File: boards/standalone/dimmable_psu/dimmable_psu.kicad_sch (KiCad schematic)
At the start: 82 parts, among them J1 DIM_IN, J2 PWM_IN, J3 POWER, J4 POWER_OUT, Q1 2N7002, Q2 IRF540N, Q3 IRF540N, U1 LM324, U2 LMC7660, U3 TPS92640

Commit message: some more pcb work
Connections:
- net GND: now also U3.15 (TP)
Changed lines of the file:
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@@
+    (stroke (width 0) (type solid) (color 0 0 0 0))
+  )
+  (wire (pts (xy 278.765 113.03) (xy 278.765 114.3))
     (stroke (width 0) (type solid) (color 0 0 0 0))
   )
@@
     )
     (property "Datasheet" "" (id 3) (at 254 119.38 0)
+      (effects (font (size 1.27 1.27)) hide)
+    )
+    (pin "1")
+  )
+  (symbol (lib_id "power:GND") (at 278.765 114.3 0) (unit 1)
+    (in_bom yes) (on_board yes)
+    (property "Reference" "#PWR?" (id 0) (at 278.765 120.65 0)
+      (effects (font (size 1.27 1.27)) hide)
+    )
+    (property "Value" "GND" (id 1) (at 279.4 119.38 0)
+      (effects (font (size 1.27 1.27)) hide)
+    )
+    (property "Footprint" "" (id 2) (at 278.765 114.3 0)
+      (effects (font (size 1.27 1.27)) hide)
+    )
+    (property "Datasheet" "" (id 3) (at 278.765 114.3 0)
       (effects (font (size 1.27 1.27)) hide)
     )
@@
     (pin "8")
     (pin "9")
+  )
+  (symbol (lib_id "Regulator_SwitchedCapacitor:LMC7660") (at 222.25 247.65 0) (unit 1)
+    (in_bom yes) (on_board yes)
+    (property "Reference" "U2" (id 0) (at 222.25 232.41 0))
+    (property "Value" "LMC7660" (id 1) (at 222.25 234.95 0))
+    (property "Footprint" "Package_SO:SOIC-8_3.9x4.9mm_P1.27mm" (id 2) (at 156.21 217.17 0)
+      (effects (font (size 1.27 1.27)) hide)
+    )
+    (property "Datasheet" "http://www.ti.com/lit/ds/symlink/lmc7660.pdf" (id 3) (at 156.21 217.17 0)
+      (effects (font (size 1.27 1.27)) hide)
+    )
+    (pin "1")
+    (pin "2")
+    (pin "3")
+    (pin "4")
+    (pin "5")
+    (pin "6")
+    (pin "7")
+    (pin "8")
   )
   (symbol (lib_id "ti_reg:TPS92640") (at 278.13 100.33 0) (unit 1)
@@
     (pin "13")
     (pin "14")
-  )
-  (symbol (lib_id "Regulator_SwitchedCapacitor:LMC7660") (at 222.25 247.65 0) (unit 1)
-    (in_bom yes) (on_board yes)
-    (property "Reference" "U2" (id 0) (at 222.25 232.41 0))
-    (property "Value" "LMC7660" (id 1) (at 222.25 234.95 0))
-    (property "Footprint" "Package_SO:SOIC-8_3.9x4.9mm_P1.27mm" (id 2) (at 156.21 217.17 0)
-      (effects (font (size 1.27 1.27)) hide)
-    )
-    (property "Datasheet" "http://www.ti.com/lit/ds/symlink/lmc7660.pdf" (id 3) (at 156.21 217.17 0)
-      (effects (font (size 1.27 1.27)) hide)
-    )
-    (pin "1")
-    (pin "2")
-    (pin "3")
-    (pin "4")
-    (pin "5")
-    (pin "6")
-    (pin "7")
-    (pin "8")
+    (pin "15")
   )
   (sheet_instances
@@
       (reference "#PWR0102") (unit 1) (value "GND") (footprint "")
     )
+    (path "/b43fa32d-11e5-4e08-bf48-f76538006246"
+      (reference "#PWR?") (unit 1) (value "GND") (footprint "")
+    )
     (path "/ce8d3fd1-9e4e-41e4-802c-895ac6841362"

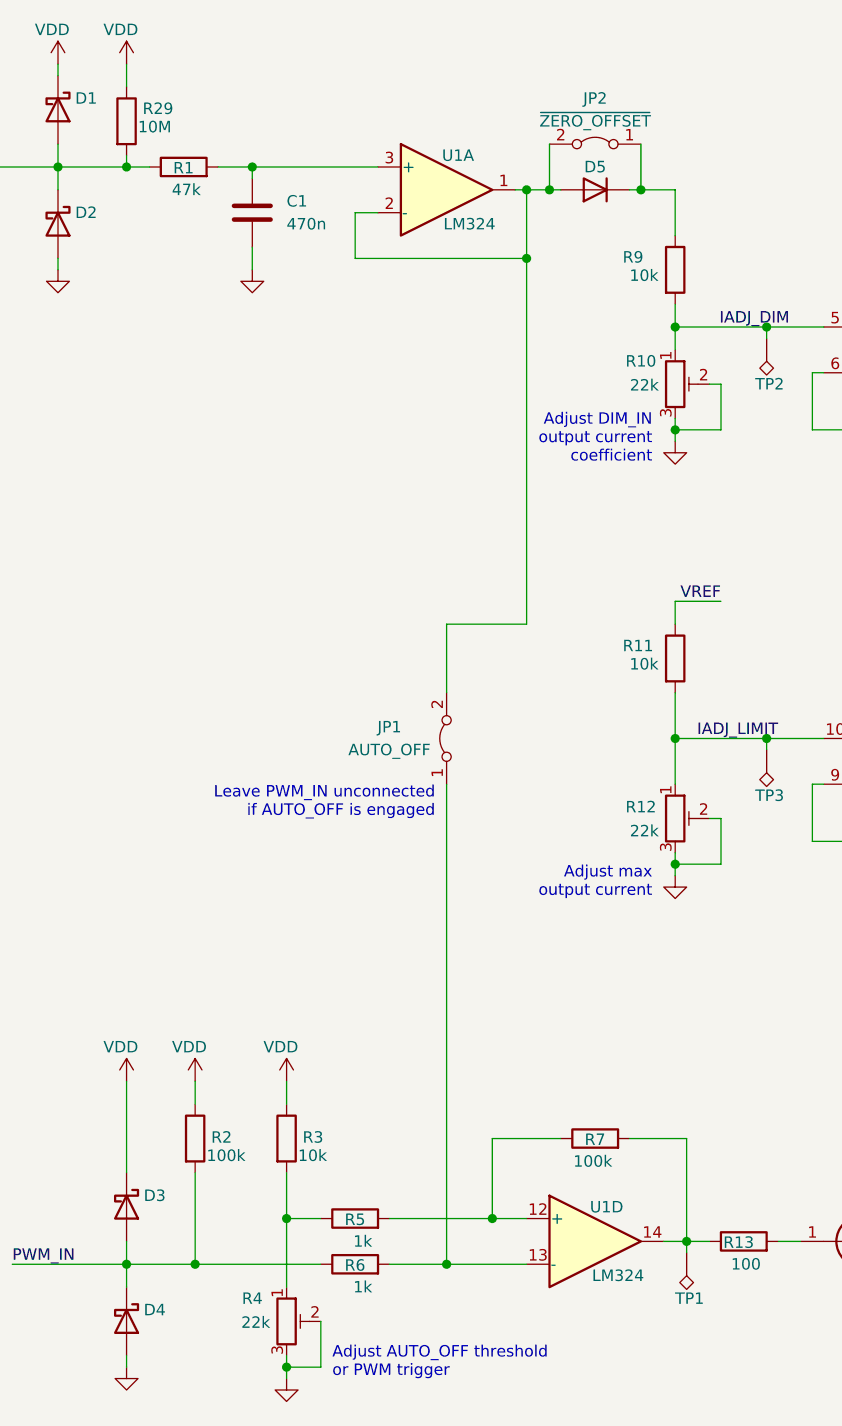
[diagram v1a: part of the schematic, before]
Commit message: use dip switches instead of jumpers
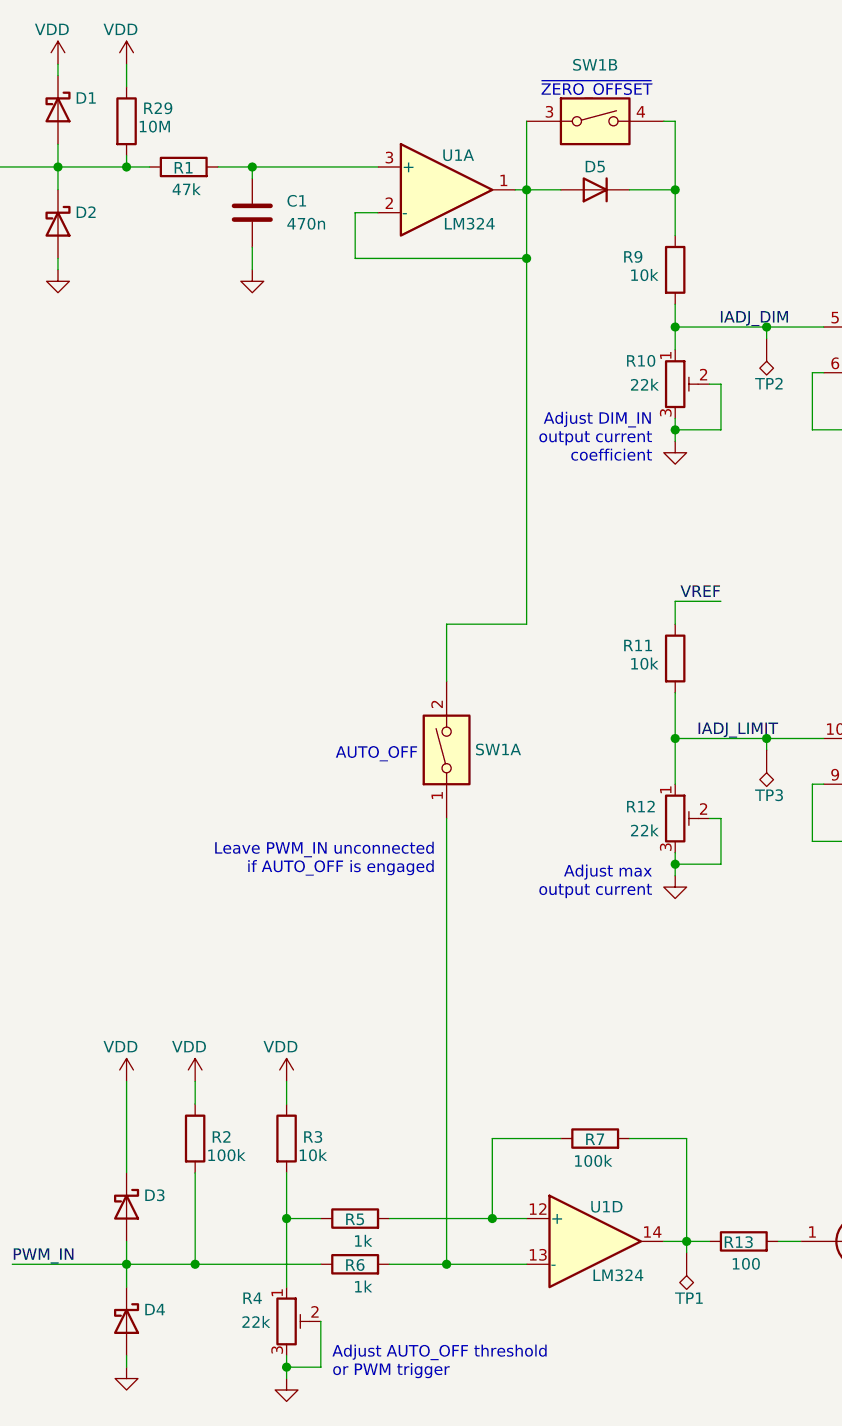
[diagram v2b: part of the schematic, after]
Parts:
- removed JP1: AUTO_OFF, Connector_PinHeader_2.54mm:PinHeader_1x02_P2.54mm_Vertical, symbol Jumper:Jumper_2_Bridged
- removed JP2: ~ZERO_OFFSET, Connector_PinHeader_2.54mm:PinHeader_1x02_P2.54mm_Vertical, symbol Jumper:Jumper_2_Bridged
- added SW1: SW_DIP_SPLIT_x02, symbol dip_switches:SW_DIP_SPLIT_x02
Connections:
- net at R6.2, U1.13 (-): now also SW1.1
- net at D5.1 (K), R9.1: now also SW1.4
- net at D5.2 (A), U1.1, U1.2 (-): now also SW1.2, SW1.3
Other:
- note added: "AUTO_OFF"
- note added: "~ZERO_OFFSET"
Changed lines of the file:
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@@
   (junction (at 104.14 48.26) (diameter 1.016) (color 0 0 0 0))
   (junction (at 104.14 55.88) (diameter 1.016) (color 0 0 0 0))
-  (junction (at 106.68 48.26) (diameter 1.016) (color 0 0 0 0))
   (junction (at 114.3 245.11) (diameter 1.016) (color 0 0 0 0))
-  (junction (at 116.84 48.26) (diameter 1.016) (color 0 0 0 0))
+  (junction (at 120.65 48.26) (diameter 1.016) (color 0 0 0 0))
   (junction (at 120.65 63.5) (diameter 1.016) (color 0 0 0 0))
   (junction (at 120.65 74.93) (diameter 1.016) (color 0 0 0 0))
@@
     (stroke (width 0) (type solid) (color 0 0 0 0))
   )
-  (wire (pts (xy 95.25 96.52) (xy 95.25 104.14))
+  (wire (pts (xy 95.25 96.52) (xy 95.25 102.87))
     (stroke (width 0) (type solid) (color 0 0 0 0))
   )
-  (wire (pts (xy 95.25 114.3) (xy 95.25 167.64))
+  (wire (pts (xy 95.25 118.11) (xy 95.25 167.64))
     (stroke (width 0) (type solid) (color 0 0 0 0))
   )
@@
     (stroke (width 0) (type solid) (color 0 0 0 0))
   )
+  (wire (pts (xy 104.14 40.64) (xy 104.14 48.26))
+    (stroke (width 0) (type solid) (color 0 0 0 0))
+  )
   (wire (pts (xy 104.14 48.26) (xy 102.87 48.26))
     (stroke (width 0) (type solid) (color 0 0 0 0))
   )
-  (wire (pts (xy 104.14 48.26) (xy 106.68 48.26))
+  (wire (pts (xy 104.14 48.26) (xy 107.95 48.26))
     (stroke (width 0) (type solid) (color 0 0 0 0))
   )
@@
     (stroke (width 0) (type solid) (color 0 0 0 0))
   )
-  (wire (pts (xy 106.68 43.18) (xy 106.68 48.26))
-    (stroke (width 0) (type solid) (color 0 0 0 0))
-  )
-  (wire (pts (xy 106.68 48.26) (xy 107.95 48.26))
-    (stroke (width 0) (type solid) (color 0 0 0 0))
-  )
   (wire (pts (xy 107.95 153.67) (xy 100.33 153.67))
     (stroke (width 0) (type solid) (color 0 0 0 0))
@@
     (stroke (width 0) (type solid) (color 0 0 0 0))
   )
-  (wire (pts (xy 115.57 48.26) (xy 116.84 48.26))
+  (wire (pts (xy 115.57 48.26) (xy 120.65 48.26))
     (stroke (width 0) (type solid) (color 0 0 0 0))
   )
@@
     (stroke (width 0) (type solid) (color 0 0 0 0))
   )
-  (wire (pts (xy 116.84 43.18) (xy 116.84 48.26))
+  (wire (pts (xy 119.38 40.64) (xy 120.65 40.64))
     (stroke (width 0) (type solid) (color 0 0 0 0))
   )
-  (wire (pts (xy 116.84 48.26) (xy 120.65 48.26))
+  (wire (pts (xy 120.65 40.64) (xy 120.65 48.26))
     (stroke (width 0) (type solid) (color 0 0 0 0))
   )
@@
     (effects (font (size 1.27 1.27)) (justify left bottom))
   )
-  (text "Leave PWM_IN unconnected\nif AUTO_OFF is engaged" (at 93.98 118.11 180)
+  (text "AUTO_OFF" (at 92.075 111.76 180)
+    (effects (font (size 1.27 1.27)) (justify right bottom))
+  )
+  (text "Leave PWM_IN unconnected\nif AUTO_OFF is engaged" (at 93.98 124.46 180)
+    (effects (font (size 1.27 1.27)) (justify right bottom))
+  )
+  (text "~ZERO_OFFSET" (at 118.11 38.1 180)
     (effects (font (size 1.27 1.27)) (justify right bottom))
   )
@@
   (symbol (lib_id "power:GND") (at 278.765 114.3 0) (unit 1)
     (in_bom yes) (on_board yes)
-    (property "Reference" "#PWR?" (id 0) (at 278.765 120.65 0)
+    (property "Reference" "#PWR0103" (id 0) (at 278.765 120.65 0)
       (effects (font (size 1.27 1.27)) hide)
     )
@@
     (pin "2")
   )
-  (symbol (lib_id "Jumper:Jumper_2_Bridged") (at 95.25 109.22 90) (unit 1)
-    (in_bom yes) (on_board yes)
-    (property "Reference" "JP1" (id 0) (at 88.9 107.95 90))
-    (property "Value" "AUTO_OFF" (id 1) (at 88.9 110.49 90))
-    (property "Footprint" "Connector_PinHeader_2.54mm:PinHeader_1x02_P2.54mm_Vertical" (id 2) (at 95.25 109.22 0)
-      (effects (font (size 1.27 1.27)) hide)
-    )
-    (property "Datasheet" "~" (id 3) (at 95.25 109.22 0)
-      (effects (font (size 1.27 1.27)) hide)
-    )
-    (pin "1")
-    (pin "2")
-  )
-  (symbol (lib_id "Jumper:Jumper_2_Bridged") (at 111.76 43.18 0) (mirror y) (unit 1)
-    (in_bom yes) (on_board yes)
-    (property "Reference" "JP2" (id 0) (at 111.76 38.1 0))
-    (property "Value" "~ZERO_OFFSET" (id 1) (at 111.76 40.64 0))
-    (property "Footprint" "Connector_PinHeader_2.54mm:PinHeader_1x02_P2.54mm_Vertical" (id 2) (at 111.76 43.18 0)
-      (effects (font (size 1.27 1.27)) hide)
-    )
-    (property "Datasheet" "~" (id 3) (at 111.76 43.18 0)
-      (effects (font (size 1.27 1.27)) hide)
-    )
-    (pin "1")
-    (pin "2")
-  )
   (symbol (lib_id "Amplifier_Operational:LM324") (at 292.1 247.65 0) (unit 5)
     (in_bom yes) (on_board yes)
@@
     (pin "3")
   )
+  (symbol (lib_id "dip_switches:SW_DIP_SPLIT_x02") (at 95.25 110.49 90) (unit 1)
+    (in_bom yes) (on_board yes)
+    (property "Reference" "SW1" (id 0) (at 100.965 110.49 90))
+    (property "Value" "SW_DIP_SPLIT_x02" (id 1) (at 91.44 110.49 0)
+      (effects (font (size 1.27 1.27)) hide)
+    )
+    (property "Footprint" "" (id 2) (at 95.25 110.49 0)
+      (effects (font (size 1.27 1.27)) hide)
+    )
+    (property "Datasheet" "~" (id 3) (at 95.25 110.49 0)
+      (effects (font (size 1.27 1.27)) hide)
+    )
+    (pin "1")
+    (pin "2")
+  )
+  (symbol (lib_id "dip_switches:SW_DIP_SPLIT_x02") (at 111.76 40.64 0) (unit 2)
+    (in_bom yes) (on_board yes)
+    (property "Reference" "SW1" (id 0) (at 111.76 34.417 0))
+    (property "Value" "SW_DIP_SPLIT_x02" (id 1) (at 111.76 36.83 0)
+      (effects (font (size 1.27 1.27)) hide)
+    )
+    (property "Footprint" "Package_DIP:DIP-4_W7.62mm_LongPads" (id 2) (at 111.76 40.64 0)
+      (effects (font (size 1.27 1.27)) hide)
+    )
+    (property "Datasheet" "~" (id 3) (at 111.76 40.64 0)
+      (effects (font (size 1.27 1.27)) hide)
+    )
+    (pin "3")
+    (pin "4")
+  )
   (symbol (lib_id "Transistor_FET:2N7002") (at 139.7 165.1 0) (unit 1)
     (in_bom yes) (on_board yes)
@@
     )
     (path "/b43fa32d-11e5-4e08-bf48-f76538006246"
-      (reference "#PWR?") (unit 1) (value "GND") (footprint "")
+      (reference "#PWR0103") (unit 1) (value "GND") (footprint "")
     )
     (path "/ce8d3fd1-9e4e-41e4-802c-895ac6841362"
@@
       (reference "J4") (unit 1) (value "POWER_OUT") (footprint "wago:2061-602")
     )
-    (path "/ba4361a7-f3c7-432b-b690-bf0d9130d7d4"
-      (reference "JP1") (unit 1) (value "AUTO_OFF") (footprint "Connector_PinHeader_2.54mm:PinHeader_1x02_P2.54mm_Vertical")
-    )
-    (path "/39d5b8a2-c05b-4322-b110-4e5678ea53a2"
-      (reference "JP2") (unit 1) (value "~ZERO_OFFSET") (footprint "Connector_PinHeader_2.54mm:PinHeader_1x02_P2.54mm_Vertical")
-    )
     (path "/62bb0cb8-bd91-46fd-bf09-993e7846f634"
       (reference "L1") (unit 1) (value "100µH") (footprint "inductors:L_Bourns_SRR1770")
@@
       (reference "R29") (unit 1) (value "10M") (footprint "Resistor_SMD:R_0805_2012Metric_Pad1.20x1.40mm_HandSolder")
     )
+    (path "/5cb36b70-e933-4478-a32f-7d281ff0571f"
+      (reference "SW1") (unit 1) (value "SW_DIP_SPLIT_x02") (footprint "")
+    )
+    (path "/70aafd63-29ed-4702-8d2b-42c6b4614284"
+      (reference "SW1") (unit 2) (value "SW_DIP_SPLIT_x02") (footprint "Package_DIP:DIP-4_W7.62mm_LongPads")
+    )
     (path "/da9b6e43-8a74-47f0-b651-737b59f893df"

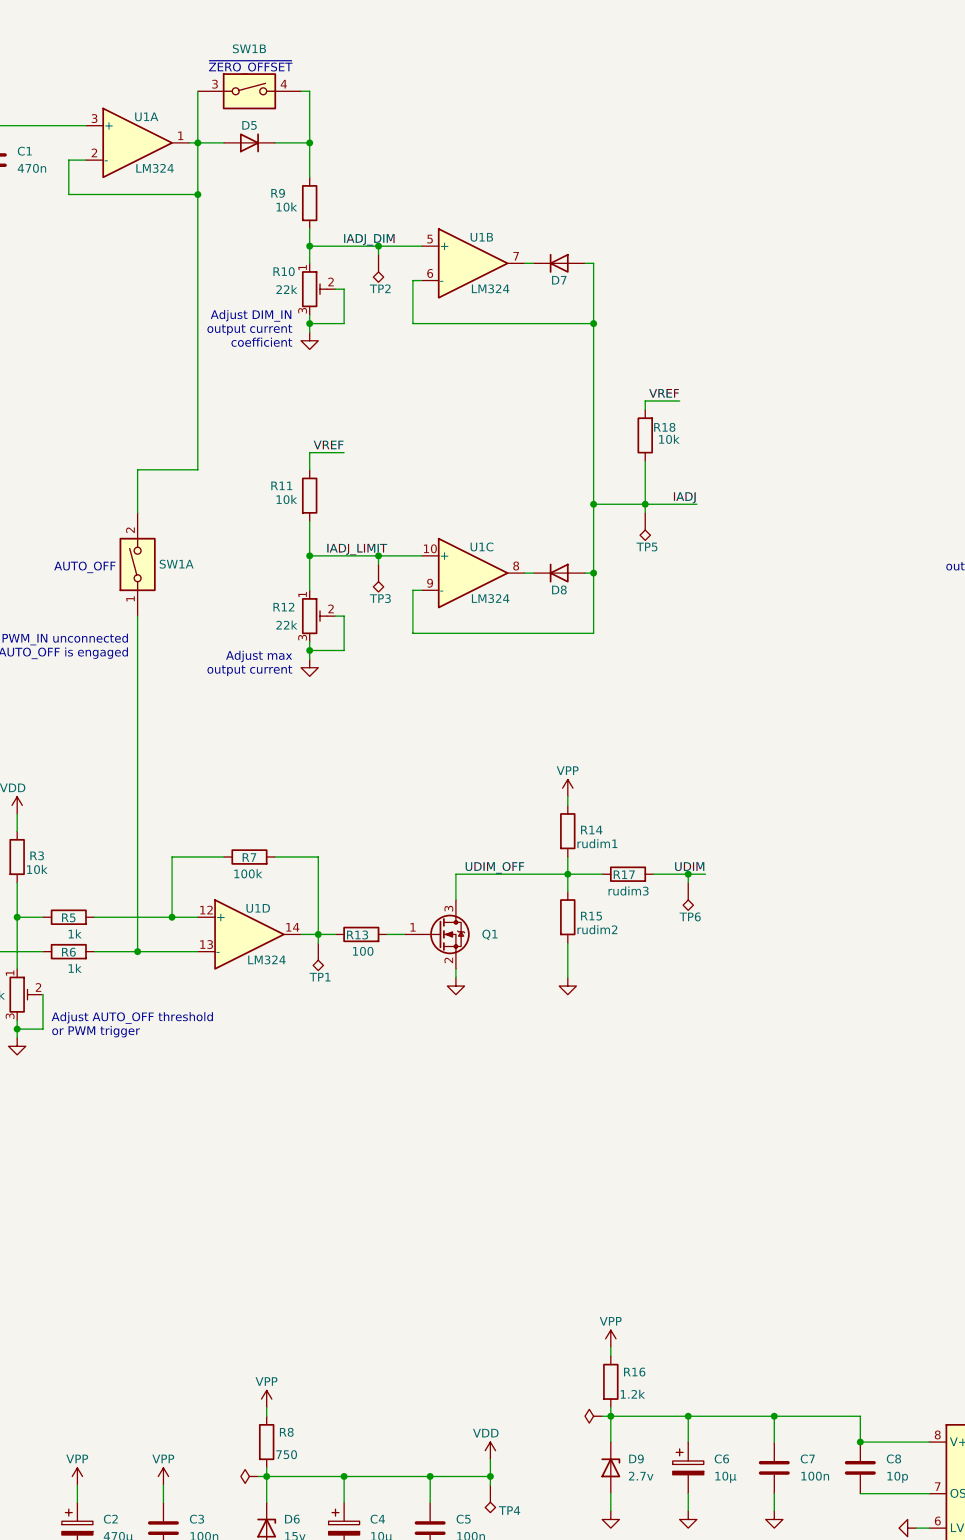
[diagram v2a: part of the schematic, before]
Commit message: some more work on dimmable psu pcb
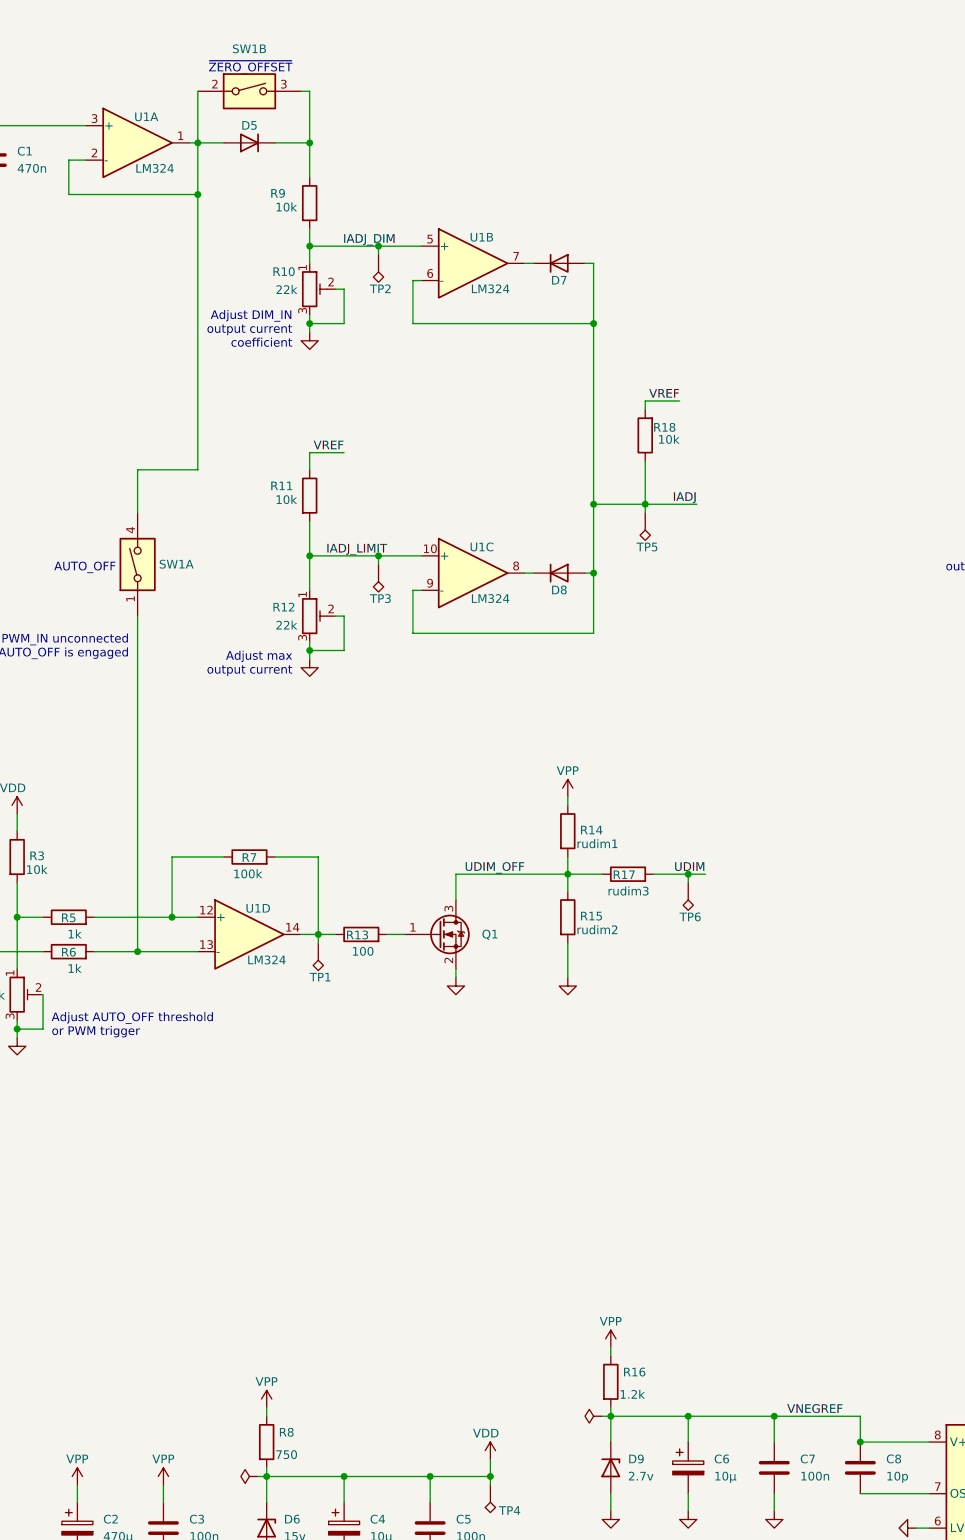
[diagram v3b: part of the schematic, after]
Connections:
- net VNEGREF: now reaches C6.1, C7.1, C8.1, D9.1 (K), R16.2, U2.8 (V+)
- net at D5.1 (K), R9.1: now also SW1.3; no longer SW1.4
- net at D5.2 (A), U1.1, U1.2 (-): now also SW1.2, SW1.4; no longer SW1.2, SW1.3
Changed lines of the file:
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@@
+    (effects (font (size 1.27 1.27)) (justify right bottom))
+  )
+  (label "VNEGREF" (at 199.39 236.22 180)
     (effects (font (size 1.27 1.27)) (justify right bottom))
   )
@@
     (pin "3")
   )
-  (symbol (lib_id "dip_switches:SW_DIP_SPLIT_x02") (at 95.25 110.49 90) (unit 1)
+  (symbol (lib_name "dip_switches:SW_DIP_SPLIT_x02_1") (lib_id "dip_switches:SW_DIP_SPLIT_x02") (at 95.25 110.49 90) (unit 1)
     (in_bom yes) (on_board yes)
     (property "Reference" "SW1" (id 0) (at 100.965 110.49 90))
@@
     )
     (pin "1")
-    (pin "2")
+    (pin "4")
   )
   (symbol (lib_id "dip_switches:SW_DIP_SPLIT_x02") (at 111.76 40.64 0) (unit 2)
@@
       (effects (font (size 1.27 1.27)) hide)
     )
+    (pin "2")
     (pin "3")
-    (pin "4")
   )
   (symbol (lib_id "Transistor_FET:2N7002") (at 139.7 165.1 0) (unit 1)
